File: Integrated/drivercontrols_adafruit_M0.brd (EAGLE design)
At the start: 68.6 x 54.3 mm, 19 parts

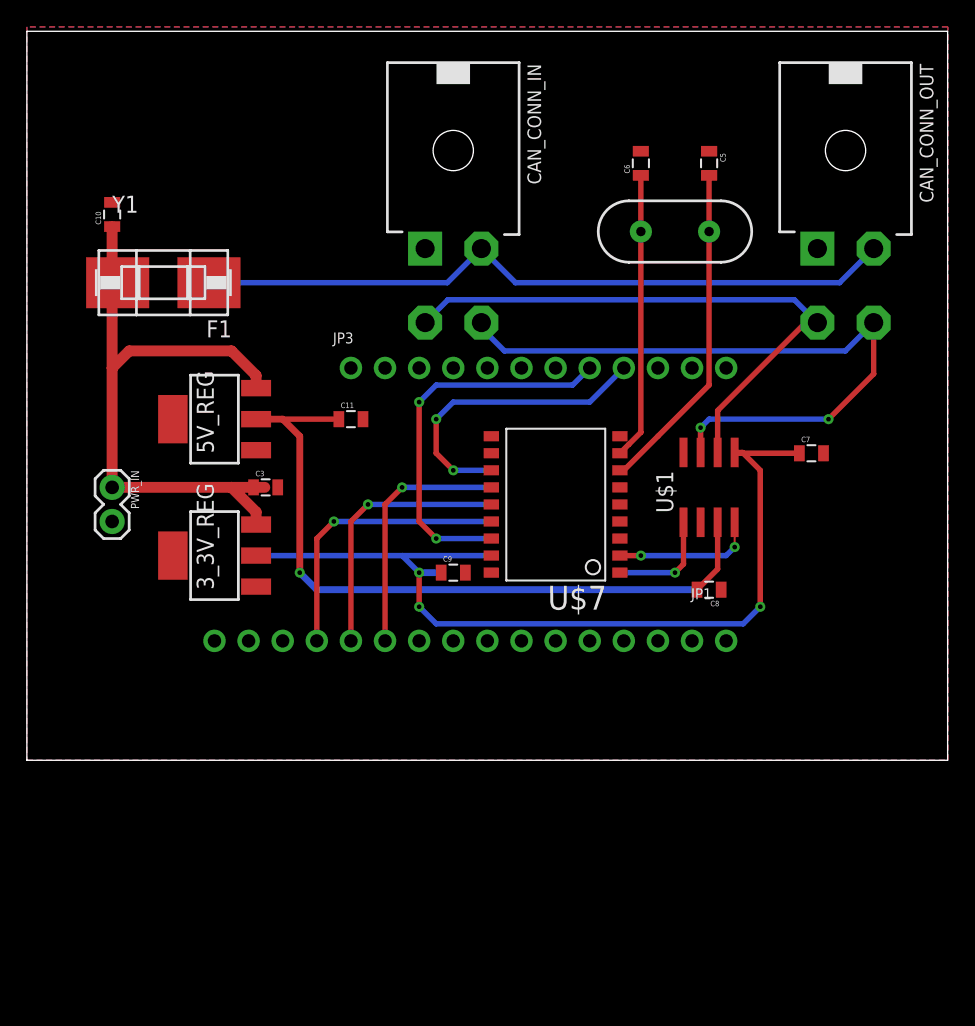
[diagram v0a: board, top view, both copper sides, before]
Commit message: left side of integrated board
has the old driver control board with the m0 addalogger board
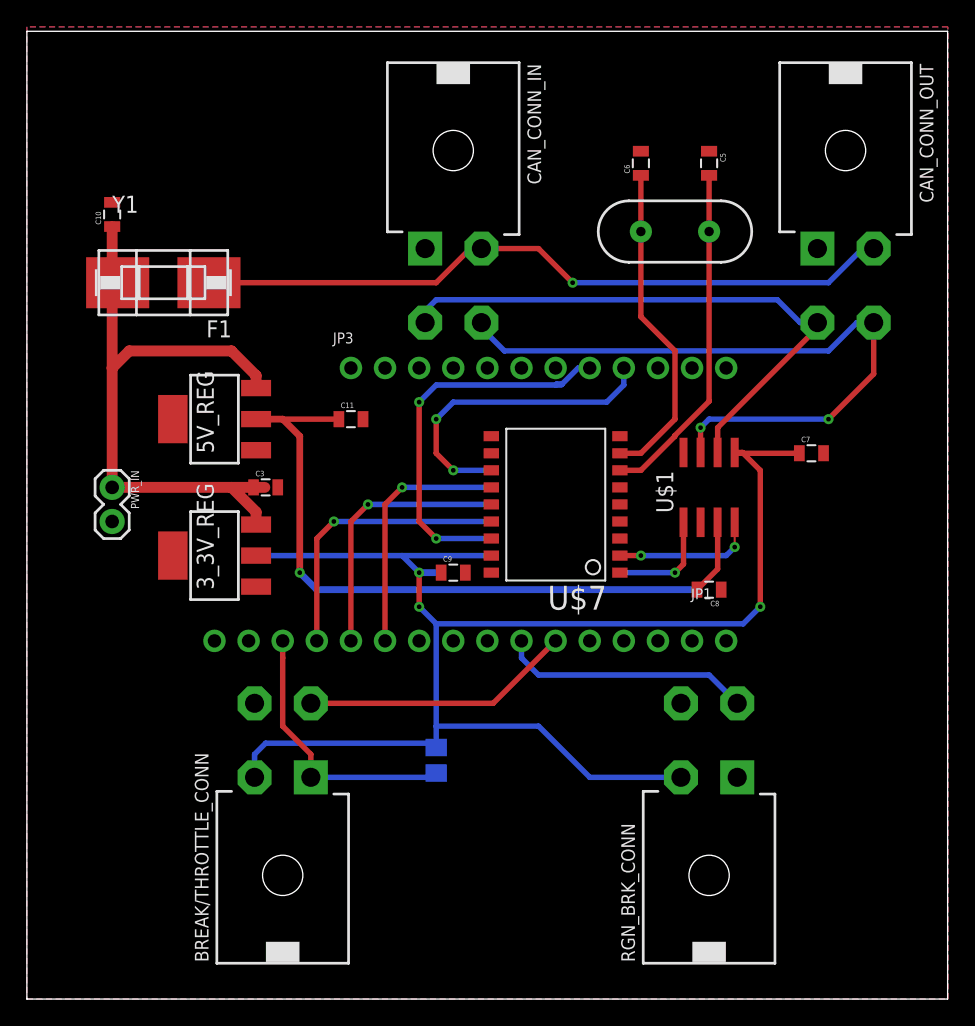
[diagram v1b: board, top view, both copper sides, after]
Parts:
- added BREAK/THROTTLE_CONN, RGN_BRK_CONN: 39-30-04?, con-molex-mini-fit:39-30-?04?
- added R1: 10K, BeagleBone_Black_Wireless:M0805
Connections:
- removed net A1: JP1.11
- removed net A2: JP1.10
- removed net D1: JP1.3
- new net BRK: BREAK/THROTTLE_CONN.1, JP1.3, R1.2
- new net RGN_BRK: JP1.10, RGN_BRK_CONN.3
- new net THROTTLE: BREAK/THROTTLE_CONN.3, JP1.11
- net 3.3V: now also BREAK/THROTTLE_CONN.2, R1.1, RGN_BRK_CONN.2
- net GND: now also BREAK/THROTTLE_CONN.4, RGN_BRK_CONN.4
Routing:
- net 3.3V: track 67.3 -> 111.6 mm
- net BRK: track 0.00 -> 20.4 mm
- net THROTTLE: track 0.00 -> 20.1 mm
- net RGN_BRK: track 0.00 -> 18.7 mm
- net N$11: track 21.3 -> 24.4 mm
- net CAN_INT: track 22.4 -> 23.2 mm
- net N$1: track 24.9 -> 25.6 mm
- net CAN+: track 52.2 -> 52.7 mm, vias 0 -> 1
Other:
- board size 68.6 x 54.3 mm -> 68.6 x 72.1 mm
